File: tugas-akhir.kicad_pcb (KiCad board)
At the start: 2 copper layers, 30 parts, among them J1 Conn_01x02_Socket, J2 Conn_01x02_Pin (solenoid lini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, K1 Relay_SPDT, M1 Stepper_Motor_bipolar / Nema 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, M2 Stepper_Motor_bipolar / Nema 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, M3 Stepper_Motor_bipolar / Nema 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, Q1 2N3904, U1 ESP32-DEVKIT-V1, U2 DCDC_StepDown_LM2596, U3 TMC2208_SILENTSTEPSTICK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

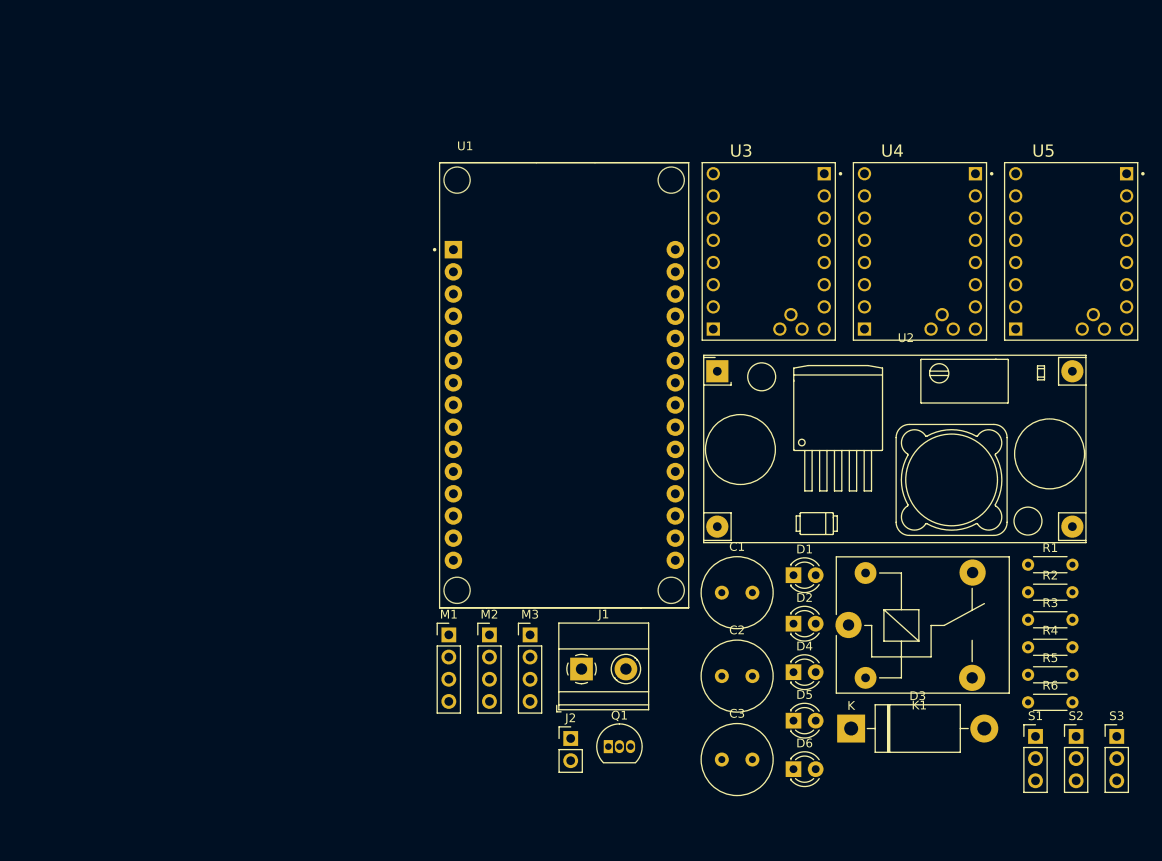
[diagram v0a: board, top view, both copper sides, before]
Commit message: route relay module
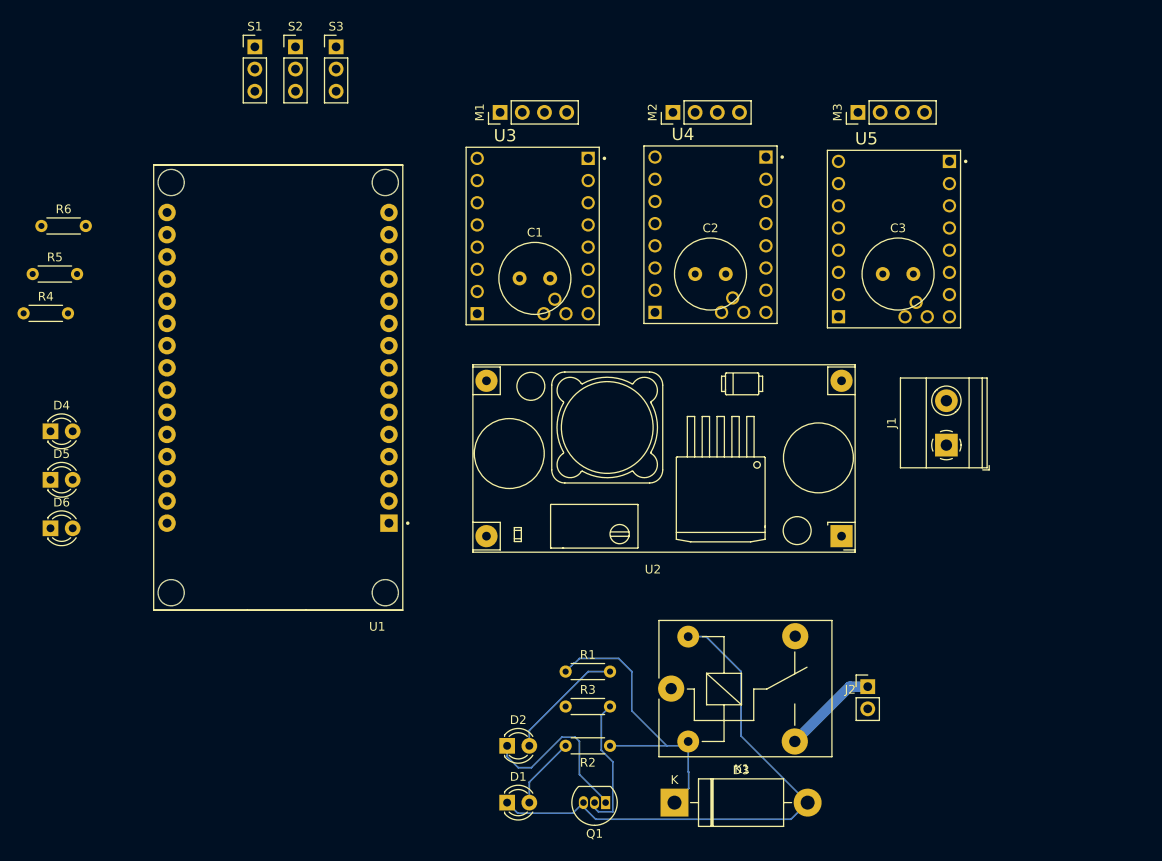
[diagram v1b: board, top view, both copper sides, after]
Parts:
- moved R6 125.4 mm to (54.9, 57.5)
- moved R5 122.8 mm to (53.9, 63.0)
- moved R4 121.2 mm to (52.9, 67.5)
- moved S1 119.2 mm to (79.3, 37.0)
- moved S2 119.2 mm to (84.0, 37.0)
- moved S3 119.2 mm to (88.7, 37.0)
- moved D4 89.4 mm to (56.0, 81.0)
- moved D5 89.4 mm to (56.0, 86.5)
- moved D6 89.4 mm to (56.0, 92.1)
- moved M3 70.6 mm to (148.4, 44.5), turned to 90 degrees
- moved M2 63.4 mm to (127.2, 44.5), turned to 90 degrees
- moved M1 60.1 mm to (107.4, 44.5), turned to 90 degrees
- moved C3 58.5 mm to (151.2, 63.0)
- moved R1 54.3 mm to (114.9, 108.5)
- moved R3 53.9 mm to (114.9, 112.5)
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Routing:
- net Net-(D1-K): track 0.00 -> 63.1 mm
- net Net-(D3-K): track 0.00 -> 35.8 mm
- net Net-(D2-K): track 0.00 -> 19.9 mm
- net Net-(Q1-B): track 0.00 -> 15.9 mm
- net Net-(D2-A): track 0.00 -> 13.8 mm
- net Net-(J2-Pin_1): track 0.00 -> 10.9 mm
- net Net-(D1-A): track 0.00 -> 8.22 mm

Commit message: update route
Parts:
- moved U2 108.9 mm to (254.8, 81.9)
- moved J1 106.4 mm to (264.3, 71.5)
- moved U1 76.9 mm to (155.5, 53.5), turned to 0 degrees
- moved S2 70.9 mm to (58.0, 103.0)
- moved S3 70.9 mm to (62.6, 103.0)
- moved S1 70.9 mm to (53.4, 103.0)
- moved M1 59.5 mm to (126.0, 101.0), turned to -90 degrees
- moved D2 52.1 mm to (151.0, 87.2), turned to -90 degrees
- moved D1 51.3 mm to (144.5, 87.2), turned to -90 degrees
- moved R1 46.9 mm to (159.5, 93.9), turned to -90 degrees
- moved R3 44.6 mm to (155.5, 93.9), turned to -90 degrees
- moved U5 37.7 mm to (122.3, 36.5), turned to 90 degrees
- moved R2 35.8 mm to (151.0, 99.0), turned to 90 degrees
- moved Q1 35.4 mm to (144.5, 98.5), turned to 90 degrees
- moved C1 34.3 mm to (127.8, 92.5), turned to 90 degrees
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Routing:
- net Net-(U1-D14): track 0.00 -> 44.5 mm
- net Net-(U1-D4): track 0.00 -> 39.3 mm
- net Net-(U1-D2): track 0.00 -> 36.2 mm
- net -24V: track 0.00 -> 29.1 mm
- net +24V: track 0.00 -> 17.8 mm
- net Net-(U5-OB1): track 0.00 -> 4.18 mm
- net Net-(U5-OB2): track 0.00 -> 4.18 mm
- net Net-(U5-OA2): track 0.00 -> 4.18 mm
- net Net-(M3--): track 0.00 -> 4.18 mm
- net Net-(U3-OB2): track 0.00 -> 4.05 mm
- net Net-(U3-OB1): track 0.00 -> 4.05 mm
- net Net-(U3-OA2): track 0.00 -> 4.05 mm
- net Net-(M1--): track 0.00 -> 4.05 mm
- net Net-(U4-OB1): track 0.00 -> 3.82 mm
- net Net-(M2--): track 0.00 -> 3.82 mm
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
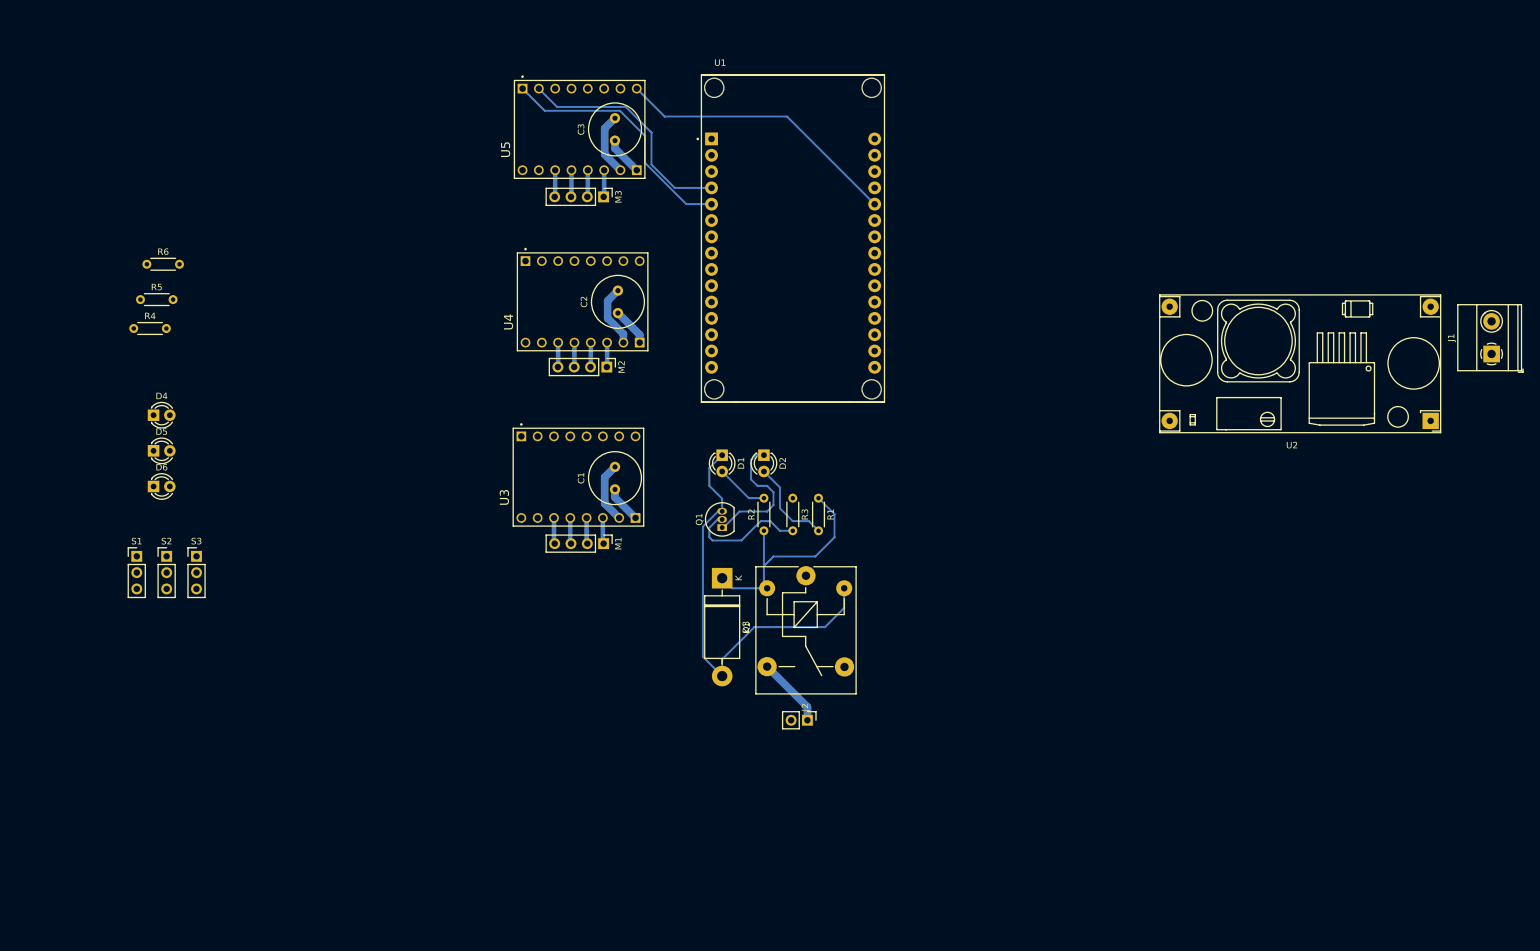
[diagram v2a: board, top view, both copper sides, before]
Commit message: route stepper driver
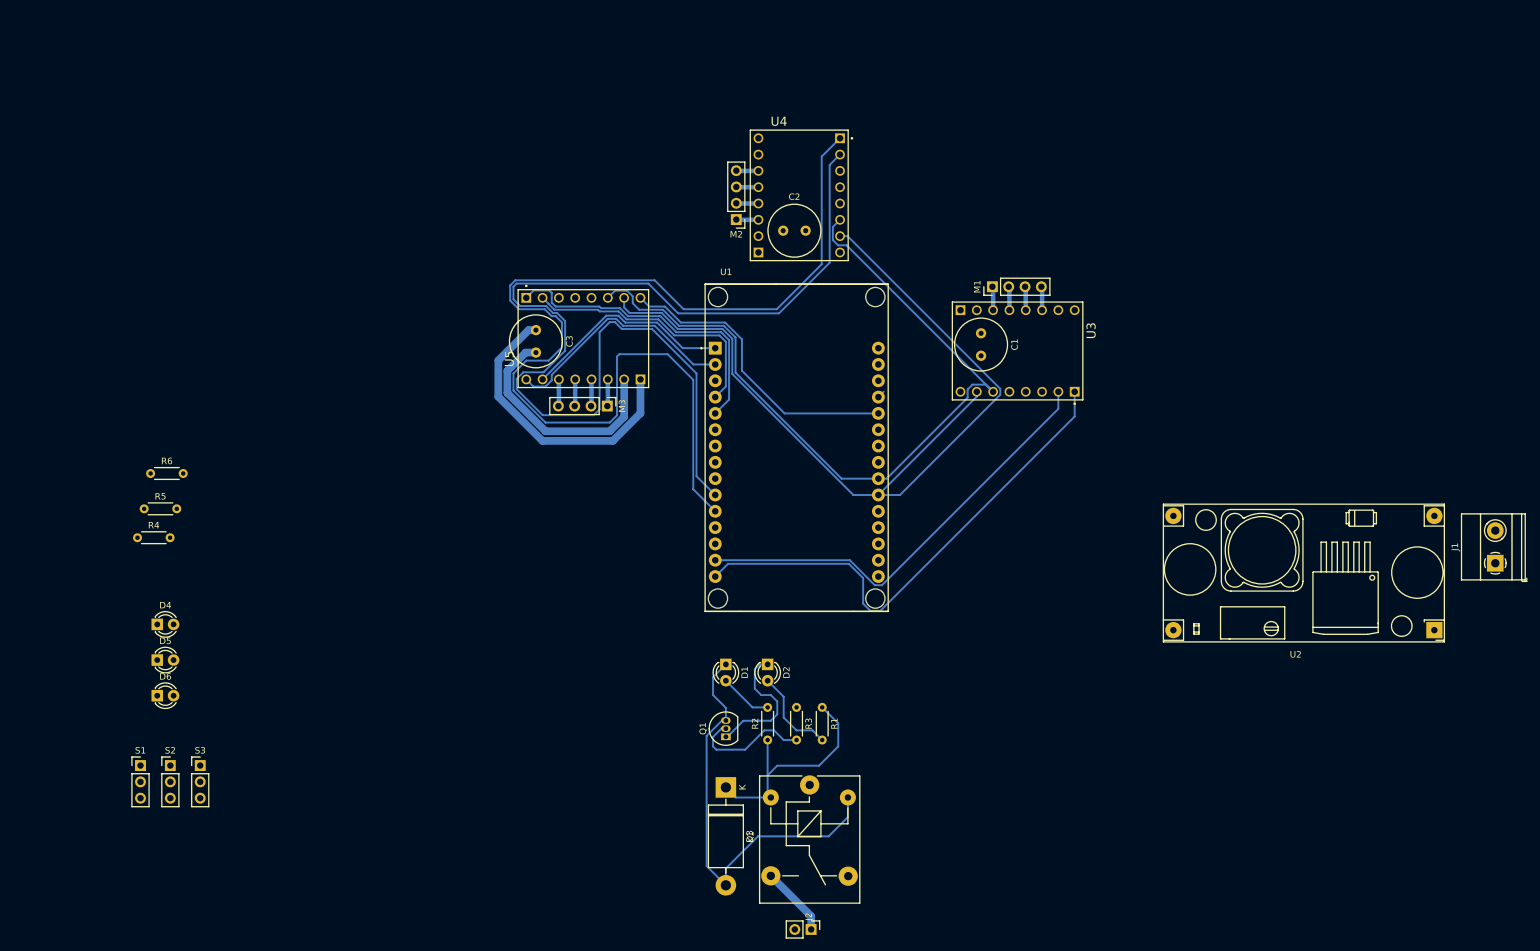
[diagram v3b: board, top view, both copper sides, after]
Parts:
- moved M1 72.6 mm to (186.6, 61.0), turned to 90 degrees
- moved U3 71.1 mm to (190.5, 71.0), turned to -90 degrees
- moved C1 62.0 mm to (184.8, 68.2), turned to -90 degrees
- moved U4 37.6 mm to (156.5, 46.8), turned to 0 degrees
- moved D3 32.6 mm to (145.1, 139.0)
- moved S1 32.6 mm to (53.9, 135.6)
- moved S2 32.6 mm to (58.6, 135.6)
- moved S3 32.6 mm to (63.2, 135.6)
- moved D1 32.6 mm to (145.1, 119.8)
- moved D2 32.6 mm to (151.6, 119.8)
- moved D4 32.6 mm to (56.5, 113.6)
- moved D5 32.6 mm to (56.5, 119.1)
- moved D6 32.6 mm to (56.5, 124.7)
- moved J1 32.6 mm to (264.9, 104.0)
- moved M3 32.6 mm to (126.6, 79.6)
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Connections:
- R3 pad 1: Net-(U1-D15) -> unconnected-(R3-Pad1)
- U1 pad 3: Net-(U1-D15) -> unconnected-(U1-D15-Pad3)
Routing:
- net Net-(U1-D21): track 0.00 -> 165.4 mm
- net Net-(U1-D19): track 0.00 -> 165.3 mm
- net Net-(U1-D32): track 0.00 -> 140.0 mm
- net Net-(U1-D33): track 0.00 -> 122.0 mm
- net Net-(U1-D23): track 0.00 -> 78.5 mm
- net Net-(U1-D22): track 0.00 -> 69.1 mm
- net Net-(D2-K): track 21.1 -> 58.8 mm
- net Net-(D3-K): track 36.8 -> 69.9 mm
- net +24V: track 17.8 -> 45.5 mm
- net Net-(U1-D4): track 39.3 -> 48.4 mm
- net -24V: track 29.1 -> 36.5 mm
- net Net-(U1-D2): track 36.2 -> 40.7 mm
- net Net-(U1-D14): track 44.5 -> 47.4 mm
- net Net-(U1-D12): track 0.00 -> 1.18 mm

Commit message: feat: new route
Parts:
- moved J1 194.5 mm to (70.5, 109.3), turned to 0 degrees
- moved U2 185.9 mm to (70.1, 99.3), turned to 90 degrees
- moved C1 151.5 mm to (38.5, 29.0)
- moved M1 149.3 mm to (42.7, 21.0)
- moved U3 149.3 mm to (46.5, 31.5)
- moved C2 115.8 mm to (38.2, 53.4), turned to -90 degrees
- moved R6 112.3 mm to (164.3, 117.5)
- moved S3 112.2 mm to (174.5, 121.4)
- moved S2 112.2 mm to (169.8, 121.4)
- moved S1 112.2 mm to (165.2, 121.4)
- moved R4 111.5 mm to (164.3, 111.2)
- moved R5 111.4 mm to (164.3, 114.4)
- moved U4 110.1 mm to (46.7, 55.9), turned to -90 degrees
- moved M2 103.9 mm to (42.9, 45.4), turned to 90 degrees
- moved M3 84.5 mm to (42.7, 69.7), turned to 90 degrees
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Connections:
- R3 pad 1: unconnected-(R3-Pad1) -> Net-(U1-D15)
- R6 pad 1: Net-(U1-D18) -> unconnected-(R6-Pad1)
- U1 pad 27: Net-(U1-D12) -> unconnected-(U1-D12-Pad27)
- U1 pad 28: Net-(U1-D13) -> unconnected-(U1-D13-Pad28)
- U1 pad 3: unconnected-(U1-D15-Pad3) -> Net-(U1-D15)
- U1 pad 8: unconnected-(U1-D5-Pad8) -> Net-(U1-D5)
- U3 pad JP1_8: Net-(U1-D12) -> Net-(U1-D21)
- U4 pad JP1_1: Net-(U1-D21) -> Net-(U1-D18)
- U4 pad JP1_8: Net-(U1-D13) -> Net-(U1-D5)
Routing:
- net Net-(U1-D32): track 140.0 -> 0.00 mm
- net Net-(U1-D33): track 122.0 -> 0.00 mm
- net Net-(U1-D21): track 165.4 -> 61.8 mm
- net Net-(U1-D5): track 0.00 -> 93.6 mm
- net Net-(U1-D19): track 165.3 -> 72.5 mm
- net Net-(U1-D18): track 0.00 -> 72.5 mm
- net Net-(D3-K): track 69.9 -> 0.00 mm
- net Net-(D1-K): track 66.9 -> 0.00 mm
- net Net-(D2-K): track 58.8 -> 0.00 mm
- net Net-(U1-D4): track 48.4 -> 0.00 mm
- net Net-(U1-D14): track 47.4 -> 0.00 mm
- net Net-(U1-D2): track 40.7 -> 0.00 mm
- net +24V: track 45.5 -> 12.2 mm
- net Net-(U1-D23): track 78.5 -> 45.5 mm
- net Net-(Q1-B): track 19.1 -> 0.00 mm
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
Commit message: finish pcb route
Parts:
- added REF**: MountingHole_3.2mm_M3, MountingHole:MountingHole_3.2mm_M3, F.Cu at (69.0, 125.2)
- added REF**: MountingHole_3.2mm_M3, MountingHole:MountingHole_3.2mm_M3, F.Cu at (216.0, 57.7)
- added REF**: MountingHole_3.2mm_M3, MountingHole:MountingHole_3.2mm_M3, F.Cu at (69.0, 57.8)
- added REF**: MountingHole_3.2mm_M3, MountingHole:MountingHole_3.2mm_M3, F.Cu at (216.0, 125.2)
- D3: footprint Diode_THT:D_DO-201AD_P15.24mm_Horizontal -> Diode_THT:D_DO-41_SOD81_P7.62mm_Horizontal
- moved J2 106.8 mm to (215.0, 93.7), turned to -90 degrees
- moved S3 95.9 mm to (97.3, 64.5)
- moved C3 87.3 mm to (121.3, 104.5), turned to 90 degrees
- moved M3 85.5 mm to (117.1, 111.8), turned to -90 degrees
- moved S1 81.8 mm to (97.3, 75.8)
- moved S2 80.1 mm to (97.3, 87.3)
- moved K1 71.6 mm to (215.2, 106.7), turned to 180 degrees
- moved U5 70.4 mm to (113.3, 101.8), turned to 90 degrees
- moved D6 70.4 mm to (187.9, 76.0), turned to 180 degrees
- moved D5 67.8 mm to (196.4, 86.0), turned to 180 degrees
- moved D3 64.1 mm to (202.3, 93.7), turned to 180 degrees
- moved U2 63.1 mm to (133.0, 95.2), turned to 0 degrees
- moved C2 54.7 mm to (73.6, 95.2)
- moved M2 54.7 mm to (78.3, 87.2)
- moved U4 54.7 mm to (82.1, 97.7)
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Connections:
- R3 pad 1: Net-(U1-D15) -> Net-(U1-D14)
- R4 pad 1: Net-(U1-D35) -> Net-(U1-D15)
- R5 pad 1: Net-(U1-D34) -> Net-(U1-D13)
- R6 pad 1: unconnected-(R6-Pad1) -> Net-(U1-D12)
- S1 pad 1: Net-(U1-D27) -> Net-(U1-D5)
- S2 pad 1: Net-(U1-D26) -> Net-(U1-TX2)
- S3 pad 1: Net-(U1-D25) -> Net-(U1-D18)
- U1 pad 27: unconnected-(U1-D12-Pad27) -> Net-(U1-D12)
- U1 pad 28: unconnected-(U1-D13-Pad28) -> Net-(U1-D13)
- U1 pad 4: Net-(U1-D2) -> unconnected-(U1-D2-Pad4)
- U1 pad 5: Net-(U1-D4) -> unconnected-(U1-D4-Pad5)
- U1 pad 7: unconnected-(U1-TX2-Pad7) -> Net-(U1-TX2)
- U3 pad JP1_6: Net-(U1-D33) -> Net-(U1-D26)
- U3 pad JP1_7: Net-(U1-D32) -> Net-(U1-D25)
- U4 pad JP1_1: Net-(U1-D18) -> Net-(U1-D34)
- U4 pad JP1_2: Net-(U1-D19) -> Net-(U1-D35)
- U4 pad JP1_6: Net-(U1-D33) -> Net-(U1-D26)
- U4 pad JP1_7: Net-(U1-D32) -> Net-(U1-D25)
- U4 pad JP1_8: Net-(U1-D5) -> Net-(U1-D19)
- U5 pad JP1_1: Net-(U1-D4) -> Net-(U1-D32)
- U5 pad JP1_2: Net-(U1-D2) -> Net-(U1-D33)
- U5 pad JP1_6: Net-(U1-D33) -> Net-(U1-D26)
- U5 pad JP1_7: Net-(U1-D32) -> Net-(U1-D25)
- U5 pad JP1_8: Net-(U1-D14) -> Net-(U1-D27)
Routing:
- net -24V: track 24.1 -> 329.8 mm
- net +24V: track 12.2 -> 296.6 mm
- net Net-(D3-K): track 0.00 -> 259.2 mm
- net Net-(D2-K): track 0.00 -> 250.0 mm
- net Net-(U1-D26): track 0.00 -> 116.9 mm
- net Net-(U1-D25): track 0.00 -> 108.0 mm
- net Net-(D1-K): track 0.00 -> 83.6 mm
- net Net-(U1-D14): track 0.00 -> 77.8 mm
- net Net-(U1-D35): track 0.00 -> 68.2 mm
- net Net-(U1-D5): track 93.6 -> 34.3 mm
- net Net-(U1-D34): track 0.00 -> 55.3 mm
- net Net-(U1-D13): track 0.00 -> 47.5 mm
- net Net-(U1-D18): track 72.5 -> 28.3 mm
- net Net-(U1-D15): track 0.00 -> 41.8 mm
- net Net-(U1-GND-Pad29): track 0.00 -> 41.8 mm
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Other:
- board outline added: 155 x 75.5 mm
